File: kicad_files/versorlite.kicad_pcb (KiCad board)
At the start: 4 copper layers, 33 x 81.3 mm, 129 parts, among them J3 RFD900ux 10 Pin Header, J4 Conn_ARM_JTAG_SWD_10, J5 RFD900ux 3 Pin Power Select, J6 USB_C_Receptacle_USB2.0_16P, J7 Micro_SD_Card_Det2, J8 Conn_01x02_Socket, J9 IGN_1, Q1 FDMC510P-MS, Q3 AO3400A, SW1 SW_Push, SW2 SW_Push, U1 STM32F407VGTx, U10 W25Q128JVS, U11 LT1963AxST-3.3, U12 AP63205WU, U13 74LVC1G125, U2 MS5611-01BA, U3 BMI088, U4 MMC5983MA, U5 MAX-M10S, U6 BMP388, U7 LSM6DSM, U9 WE-TVS-82400102, Y1 LFXTAL036869Reel 8MHz Crystal

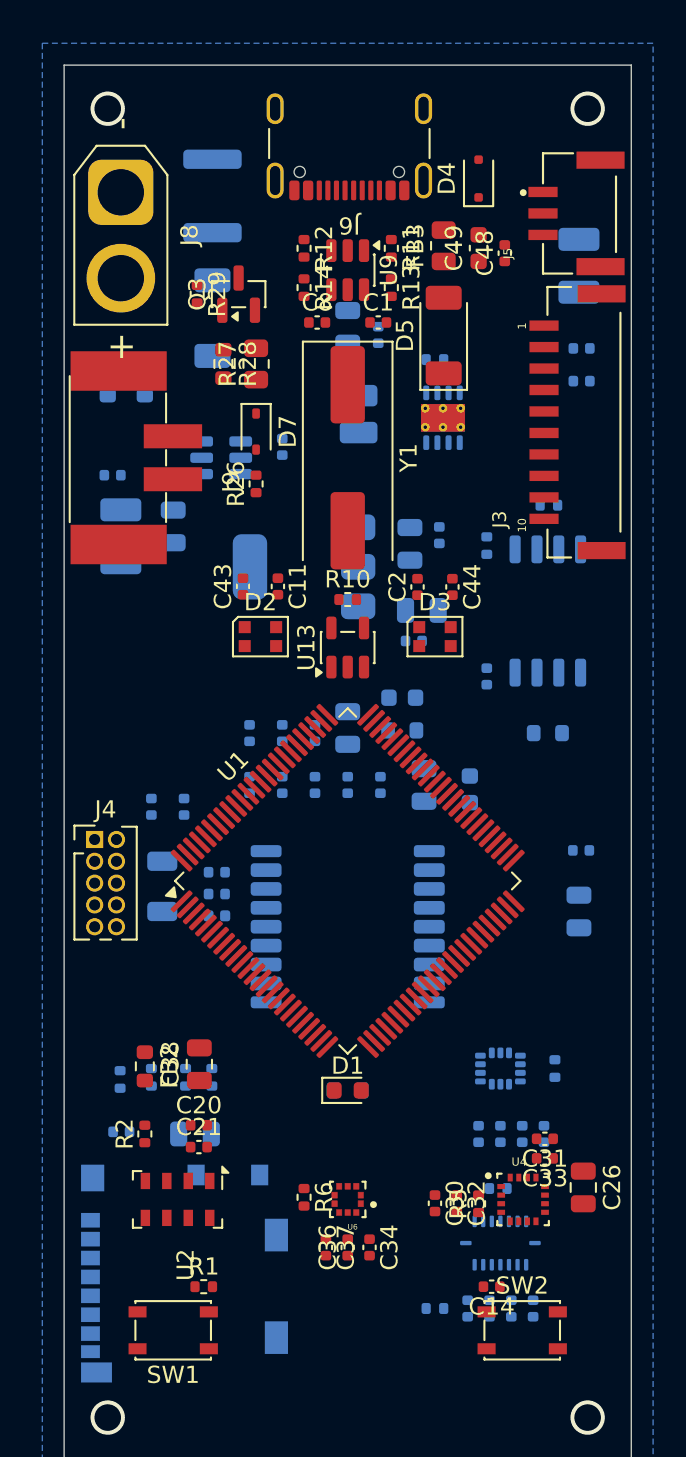
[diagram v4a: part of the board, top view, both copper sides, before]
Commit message: Test route, place some GND vias
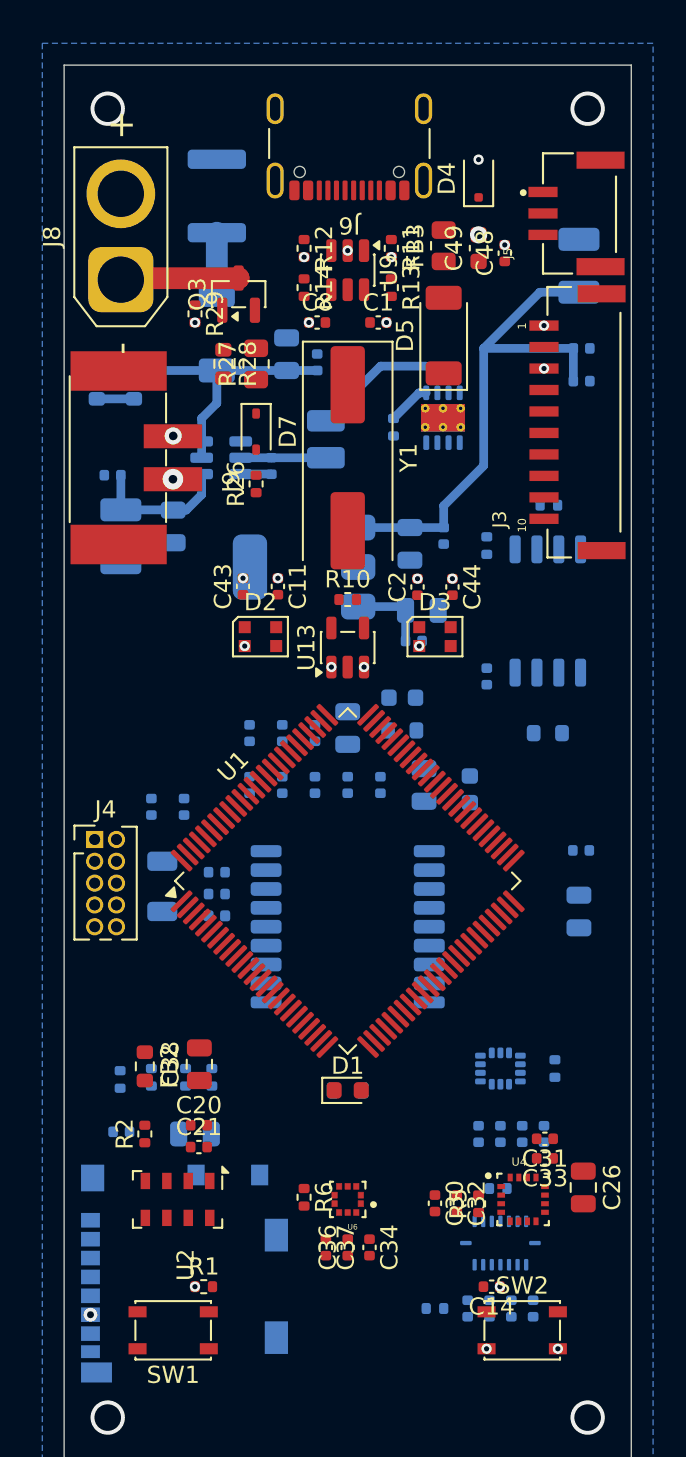
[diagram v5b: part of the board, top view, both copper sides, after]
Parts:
- moved J8 5.09 mm to (130.3, 74.7), turned to 90 degrees
- moved R22 4.62 mm to (146.2, 83.3), turned to -90 degrees
- moved C61 3.90 mm to (141.7, 79.5)
- moved C62 3.90 mm to (140.0, 79.1)
- moved L1 2.40 mm to (142.2, 84.0), turned to -90 degrees
- moved C60 1.28 mm to (139.1, 85.6)
- moved R29 1.15 mm to (134.6, 76.7)
- moved D8 0.89 mm to (135.9, 77.8)
- moved R24 0.66 mm to (131.1, 80.8)
- moved R25 0.66 mm to (128.9, 80.8)
- moved C55 0.26 mm to (149.1, 89.6)
- moved F1 0.25 mm to (135.9, 69.8)
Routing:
- net +5V: track 0.00 -> 30.4 mm
- net Net-(D8-K): track 0.00 -> 16.1 mm
- net Net-(Q1-S): track 0.00 -> 15.5 mm
- net +9V: track 0.00 -> 6.86 mm
- net Net-(U12-SW): track 0.00 -> 4.96 mm
- net +3.3V_MAIN: track 0.00 -> 4.63 mm
- net Net-(D8-A): track 0.00 -> 3.62 mm
- net /Power/+VBUS: track 0.00 -> 2.52 mm
- net /MCU/BATT_READ: track 0.00 -> 2.16 mm
- net Net-(U12-BST): track 0.00 -> 1.79 mm
- net Net-(J9-Pin_2): vias 0 -> 1
- net GND: vias 0 -> 25

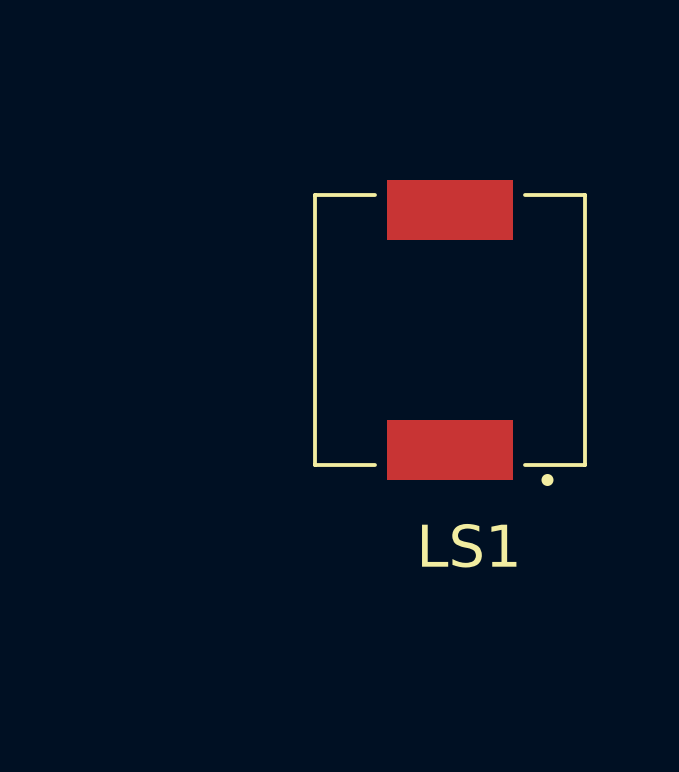
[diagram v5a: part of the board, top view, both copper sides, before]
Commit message: Remove obsolete footprint
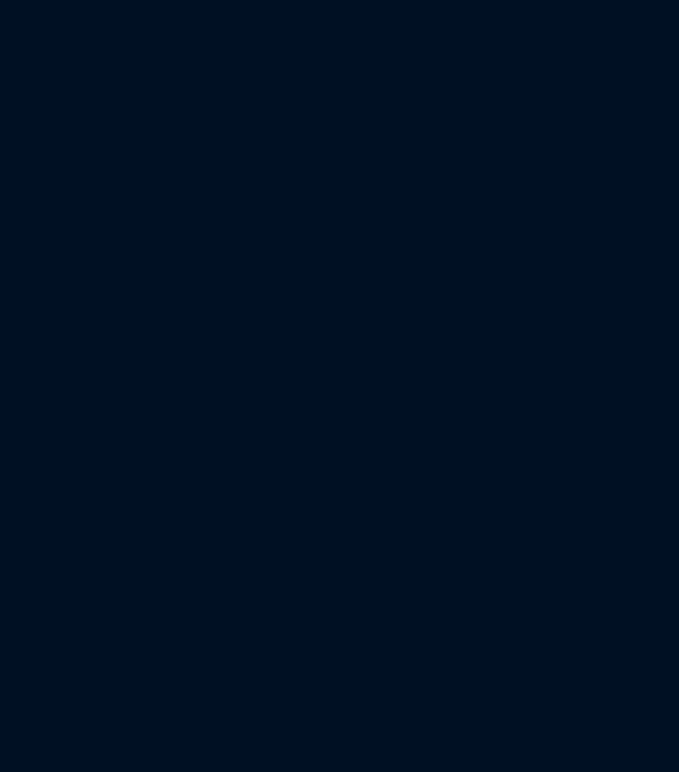
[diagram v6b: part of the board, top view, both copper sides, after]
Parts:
- removed LS1: CMT-4023S-SMT-TR, footprints:CUI_CPT-9019S-SMT

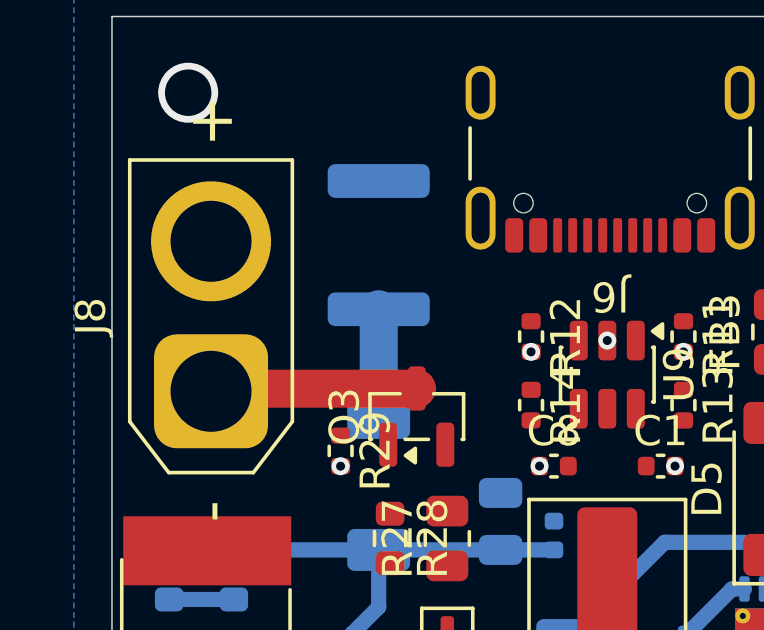
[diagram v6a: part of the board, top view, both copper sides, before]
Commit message: That was NOT supposed to be there
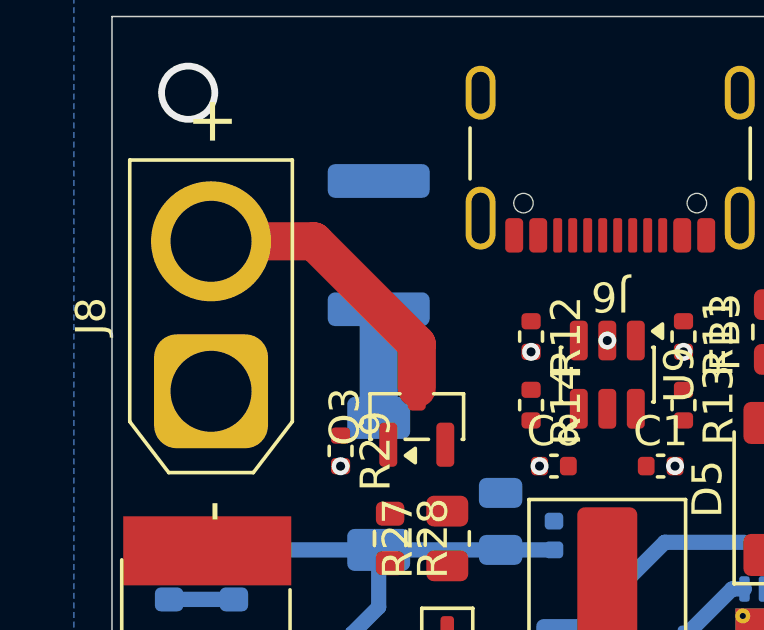
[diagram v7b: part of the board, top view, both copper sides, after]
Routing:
- net +9V: track 6.86 -> 9.75 mm
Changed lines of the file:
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@@
 	)
 	(segment
-		(start 130.302 74.636)
-		(end 137.151499 74.636)
+		(start 137.16 73.152)
+		(end 133.731 69.723)
 		(width 1.27)
 		(layer "F.Cu")
@@
 	)
 	(segment
-		(start 137.151499 74.636)
-		(end 137.16 74.627499)
+		(start 133.731 69.723)
+		(end 130.302 69.723)
 		(width 1.27)
 		(layer "F.Cu")
+		(net "+9V")
+	)
+	(segment
+		(start 137.16 74.627499)
+		(end 137.16 73.152)
+		(width 1.27)
+		(layer "F.Cu")

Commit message: GND layer to In2 in stackup
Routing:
- added copper zone on In2.Cu, net GND
- removed copper zone on In1.Cu, net GND
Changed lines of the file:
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@@
 	(zone
 		(net "GND")
-		(layer "In1.Cu")
+		(layer "In2.Cu")
 		(name "GND")
 		(hatch edge 0.5)
@@
 		(polygon
 			(pts
-				(xy 125.73 60.96) (xy 125.73 144.78) (xy 161.29 144.78) (xy 161.29 60.96)
+				(xy 124.46 59.69) (xy 162.56 59.69) (xy 162.56 146.05) (xy 124.46 146.05)
 			)
 		)
